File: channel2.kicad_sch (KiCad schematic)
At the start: 58 parts, among them IC3 TLV73325PDBVT, IC4 TLV73312PDBVT, J4 HDMI-A_Molex_471511001, J5 5051101992, U4 TC358742XBG, U5 TPD8S009DSMR, U6 PCA9517ATP, Y2 Oscillator_27MHz_TXC_7C

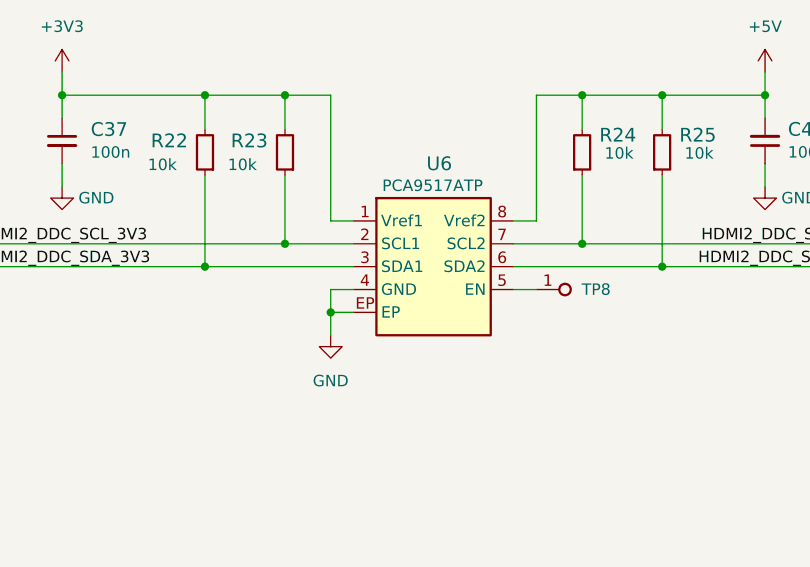
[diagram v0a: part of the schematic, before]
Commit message: [#58304] Update PCA9517ATP symbol
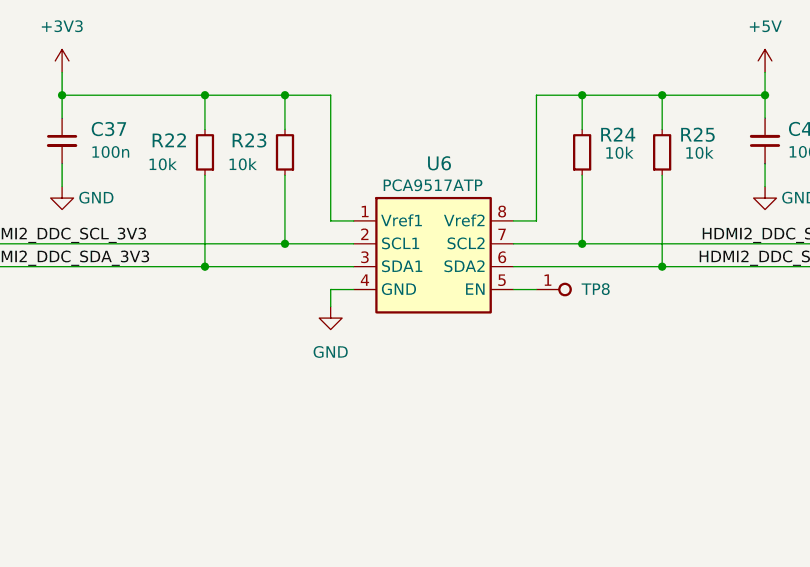
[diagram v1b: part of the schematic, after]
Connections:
- net GND: now also U6.9 (GND); no longer U6.EP
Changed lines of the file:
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@@
   (junction (at 214.63 260.35) (diameter 0) (color 0 0 0 0)
   )
-  (junction (at 335.28 109.22) (diameter 0) (color 0 0 0 0)
-  )
   (junction (at 186.69 240.03) (diameter 0) (color 0 0 0 0)
   )
@@
     (stroke (width 0) (type default))
   )
-  (wire (pts (xy 335.28 109.22) (xy 337.82 109.22))
-    (stroke (width 0) (type default))
-  )
   (wire (pts (xy 151.13 67.945) (xy 167.64 67.945))
     (stroke (width 0) (type default))
@@
     (stroke (width 0) (type default))
   )
-  (wire (pts (xy 335.28 109.22) (xy 335.28 106.68))
+  (wire (pts (xy 335.28 106.68) (xy 335.28 108.585))
     (stroke (width 0) (type default))
   )
@@
     (stroke (width 0) (type default))
   )
-  (wire (pts (xy 335.28 109.22) (xy 335.28 111.76))
-    (stroke (width 0) (type default))
-  )
   (wire (pts (xy 186.69 240.03) (xy 192.405 240.03))
     (stroke (width 0) (type default))
@@
     )
   )
-  (symbol (lib_id "antmicropower:GND") (at 335.28 111.76 0) (mirror y) (unit 1)
+  (symbol (lib_id "antmicropower:GND") (at 335.28 108.585 0) (mirror y) (unit 1)
     (in_bom yes) (on_board yes) (dnp no) (fields_autoplaced)
-    (property "Reference" "#PWR0169" (at 335.28 118.11 0)
+    (property "Reference" "#PWR0169" (at 335.28 114.935 0)
       (effects (font (size 1.27 1.27)) hide)
     )
-    (property "Value" "GND" (at 335.28 116.84 0)
+    (property "Value" "GND" (at 335.28 113.665 0)
       (effects (font (size 1.27 1.27)))
     )
-    (property "Footprint" "" (at 335.28 111.76 0)
+    (property "Footprint" "" (at 335.28 108.585 0)
       (effects (font (size 1.27 1.27)) hide)
     )
-    (property "Datasheet" "" (at 335.28 111.76 0)
+    (property "Datasheet" "" (at 335.28 108.585 0)
       (effects (font (size 1.27 1.27)) hide)
     )
@@
       (effects (font (size 1.524 1.524)))
     )
-    (property "Value" "PCA9517ATP" (at 341.63 95.885 0)
-      (effects (font (size 1.27 1.27) (thickness 0.15)) (justify left bottom) hide)
+    (property "Value" "PCA9517ATP" (at 340.995 95.885 0)
+      (effects (font (size 1.27 1.27) (thickness 0.15)) (justify left bottom))
     )
     (property "Footprint" "antmicro-footprints:SOT1069-2" (at 370.84 106.68 0)
@@
       (effects (font (size 1.27 1.27) (thickness 0.15)) (justify left bottom) hide)
     )
-    (property "MPN" "PCA9517ATP" (at 340.995 95.885 0)
-      (effects (font (size 1.27 1.27) (thickness 0.15)) (justify left bottom))
+    (property "MPN" "PCA9517ATP" (at 370.84 111.76 0)
+      (effects (font (size 1.27 1.27) (thickness 0.15)) (justify left bottom) hide)
     )
     (property "Manufacturer" "NXP" (at 370.84 114.3 0)
@@
     (pin "7")
     (pin "8")
-    (pin "EP")
+    (pin "9")
     (instances
       (project "antmicro-hdmi-mipi-bridge-hw"

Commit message: [#58304] kmake dnp
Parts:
- J5: DNP (none) -> DNP
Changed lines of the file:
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@@
       (effects (font (size 1.27 1.27) (thickness 0.15)) (justify left bottom) hide)
+    )
+    (property "DNP" "DNP" (at 0.0 0.0 0)
+      (effects (font (size 1.0 1.0)))
     )
     (pin "1")
@@
     (pin "8")
     (pin "9")
-    (pin "8")
-    (instances
-      (project "antmicro-hdmi-mipi-bridge-hw"
+    (instances
+      (project "antmicro-hdmi-mipi-bridge-hw"
